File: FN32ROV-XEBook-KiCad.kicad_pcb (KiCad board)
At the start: 2 copper layers, 66 x 56 mm, 64 parts, among them J2 USB-C 16P, Q1 UMH3NTN, Q2 DMP2035U-7, Q3 DMG2302U, U1 ESP32-WROVER-IE-N16R8, U2 CP2102N-A02-GQFN24R, U3 74LS07DR, U4 74LS07DR, U5 XC6220B331MR

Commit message: Resize R13 to 2.7k for the LED boards green WiFi LED, document the LED board interface
The WiFi status LED moved to the new FN32ROV-XEBook-LED-KiCad daughter board and
changed color from white to green, which has a lower forward voltage (~2.2V vs
~2.9V). R13 needed to grow from 1k to 2.7k to keep the current in the same range
as the original design. Also documents the sibling LED board repo and the
per-channel resistor rationale in CLAUDE.md.

Co-Authored-By: Claude Sonnet 5 <noreply@anthropic.com>
Claude-Session: https://claude.ai/code/session_011E5FphyrLWBpYvbXpCPZfr
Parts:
- R13: value 1k -> 2.7k
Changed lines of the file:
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@@
 			)
 		)
-		(property "Value" "1k"
+		(property "Value" "2.7k"
 			(at 0 1.17 0)
 			(layer "F.Fab")
+			(hide yes)
 			(effects
 				(font
@@
 			(at 0 1.17 0)
 			(layer "F.Fab")
-			(effects
-				(font
+			(hide yes)
+			(effects
+				(font

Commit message: Replace D7/D8 diode part to fix SOD-323/SOD-123W package mismatch
PCBWay's assembly review caught that PMEG2010ER,115 (the part specified
for D7/D8) is only manufactured in SOD-123W, not the SOD-323 footprint
used on this board. Rather than swap the PCB footprint (which would
require re-routing around a nearby USB_D+ trace and re-exporting
gerbers), swapped the part instead: Nexperia PMEG2010BEA,115
(LCSC C455041) is a direct electrical equivalent (20V/1A Schottky, low
Vf) genuinely packaged in SOD-323, matching the existing footprint.
Board layout and gerbers are unaffected (value text lives on F.Fab).

Also includes the filled-in Customer Reply column for PCBWay's BOM
quote questions (this diode fix, three benign capacitor voltage-rating
upgrades, sourcing for J_SIO1, and flagging that their R13 quote used a
stale pre-2.7k BOM revision).

Co-Authored-By: Claude Sonnet 5 <noreply@anthropic.com>
Claude-Session: https://claude.ai/code/session_01GM9FQ1pLMMKCV3Qfiq1ore
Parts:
- D7, D8: value PMEG2010ER,115 -> PMEG2010BEA,115
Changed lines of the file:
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@@
 			(at 0 3.23 0)
 			(layer "F.Fab")
+			(hide yes)
 			(effects
 				(font
@@
 			)
 		)
-		(property "Value" "PMEG2010ER,115"
+		(property "Value" "PMEG2010BEA,115"
 			(at 0.1 1.9 90)
 			(layer "F.Fab")
@@
 			)
 		)
-		(property "Value" "PMEG2010ER,115"
+		(property "Value" "PMEG2010BEA,115"
 			(at 0.1 1.9 90)
 			(layer "F.Fab")

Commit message: Ground the copper pour, finish the plane, and archive the as-built 1.0 package
The single F.Cu/B.Cu zone was (net 0) -- a floating flood, not a ground plane.
Assign it to /GND and complete it:

- 65 stitching vias on a 3mm grid (GND vias 4 -> 177), placed by deflating the
  filled zone polygon 0.75mm per layer and intersecting F.Cu with B.Cu, so every
  candidate is inherently clearance-safe
- island_removal_mode -> Always, clearing 67 isolated_copper warnings
- min_resolved_spokes 2 -> 1; D4.2 and C4.1 set to solid zone connection

81 -> 8 DRC violations, 0 unconnected. Strictly additive: 64 footprint positions
byte-identical, tracks 894 -> 894, outline 66.050 x 56.050mm unchanged to 0.1um,
because the mounting brackets are already fabricated.

Fab/ restructured: the exact package sent to PCBWay is frozen under
as-built-1.0-PCBWay-T-1D22W845207A/ with the quote correspondence, and the new
Gerbers-FN32ROV-XEBook-1.1/ sits alongside it. 1.1 differs from 1.0 only in
F.Cu, B.Cu and the PTH drill (+65 hits); mask, paste, silkscreen and Edge.Cuts
are byte-identical, and BOM/CPL are copied verbatim.

PCBWay declined the mid-order swap on 2026-08-02 -- the boards were already in
manufacturing -- so 1.1 has never been fabricated and is future-order-only.
The ordered boards still work: verified 0 unconnected, 59 GND pads tied by 188
track/via segments. GND was fully routed in copper precisely because the pour
carried no net, so nothing depended on it.

Also adds the SIO/SD cable wiring PDFs under Docs/.

Co-Authored-By: Claude Opus 5 <noreply@anthropic.com>
Claude-Session: https://claude.ai/code/session_01VRTanwY2PaFNJQ1vUGmami
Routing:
- net /GND: vias 4 -> 69
- added copper zone on B.Cu, net /GND
- added copper zone on F.Cu, net /GND
- removed copper zone on B.Cu, net (none)
- removed copper zone on F.Cu, net (none)

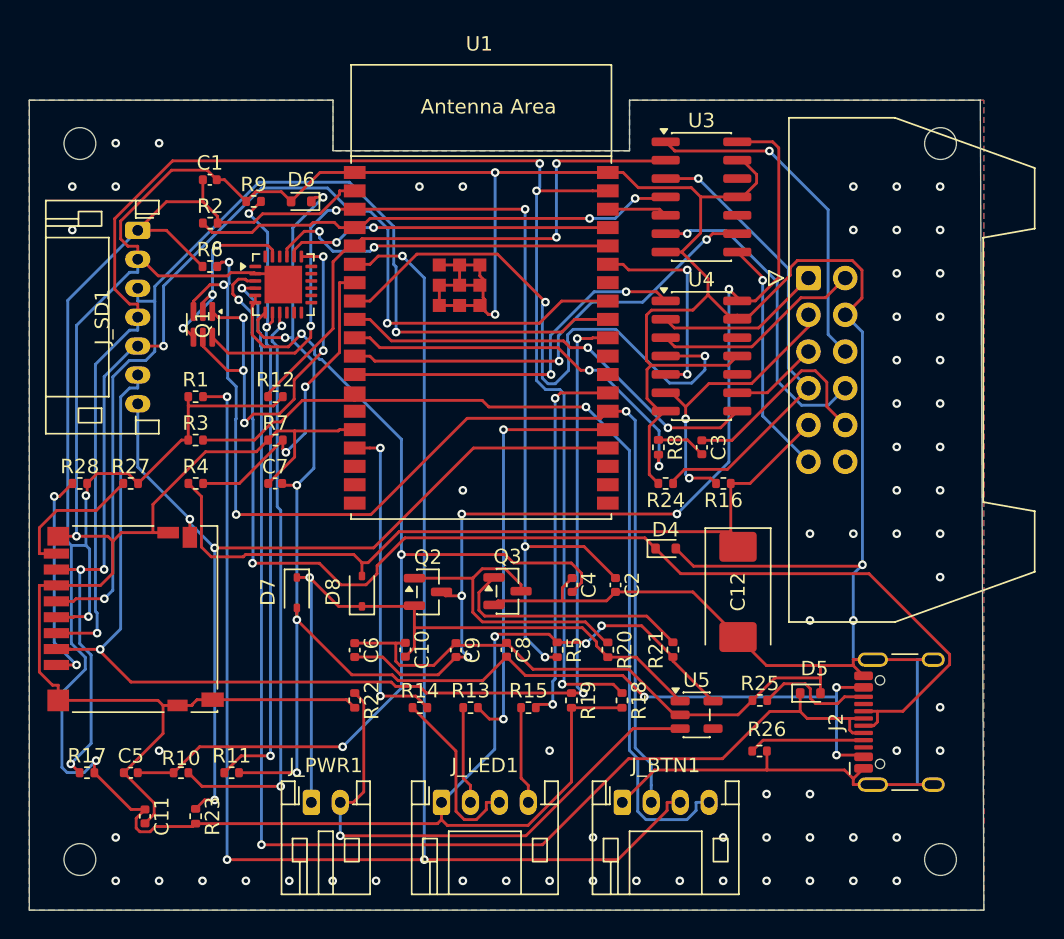
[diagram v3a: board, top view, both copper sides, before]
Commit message: Match LED brightness (R14 30k, R15 10K) and re-export fab for PCBWay
WiFi (R13 2.7k, green) was the channel the build is happy with; BT and SIO
read about twice as bright. Values come from a bench match on the LED board
at 3.33V with WiFi through its real 2.7k, not from calculation -- estimates
based on the 50%-dimming tape used as a stopgap landed near 2.4k and were
far off. The visual match was 9.2k on SIO; 10K was chosen deliberately as
slightly dimmer and already a basic part on this board.

  R13 WiFi green   2.7k  unchanged  C413089
  R14 BT   blue    1k -> 30k        C25776
  R15 SIO  orange  1.2k -> 10K      C25744

The 1.0 boards still carry 1k/1.2k and need hand-rework (0402s at y=67).

Fab re-export (Gerbers-FN32ROV-XEBook-1.1, never fabricated, so updated in
place): copper and drill came out identical to the 2026-08-01 export, which
also confirms the post-autoroute copper restore is exact. Only F.Silkscreen
changed, picking up the D4-D8 cathode bars and the corrected J_SIO1 vertical
header that were fixed in source after that export. Pick-and-place positions
and rotations are unchanged from what PCBWay assembled on 1.0.

Adds FN32ROV-XEBook-KiCad-BOM-PCBWay.xlsx/.csv as the file to send PCBWay:
same-part designators on one row (their explicit request), actual purchased
MPNs, the higher-voltage caps they substituted, J_SIO1 as BOOMELE 2.54-2*6P
(C9136), R13 on its own line. Verified against the schematic BOM and
pick-and-place: 60 placements, 28 lines. The plain BOM is now exported from
the schematic rather than hand-maintained.

Also folds in uncommitted work from earlier sessions: U1 -> ESP32-WROVER-E-
N16R8 (C529589) for the working PCB antenna, J_SIO1 -> Connector_IDC vertical
footprint, the unused Latch_Horizontal override's silk, removal of the two
superseded cable PDFs, and PCBWay's rev-1.0 question photos (D4/D5/D6 and
J_SIO1 orientation). .dsn is now gitignored as a regenerable export.

Co-Authored-By: Claude Opus 5 (1M context) <noreply@anthropi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
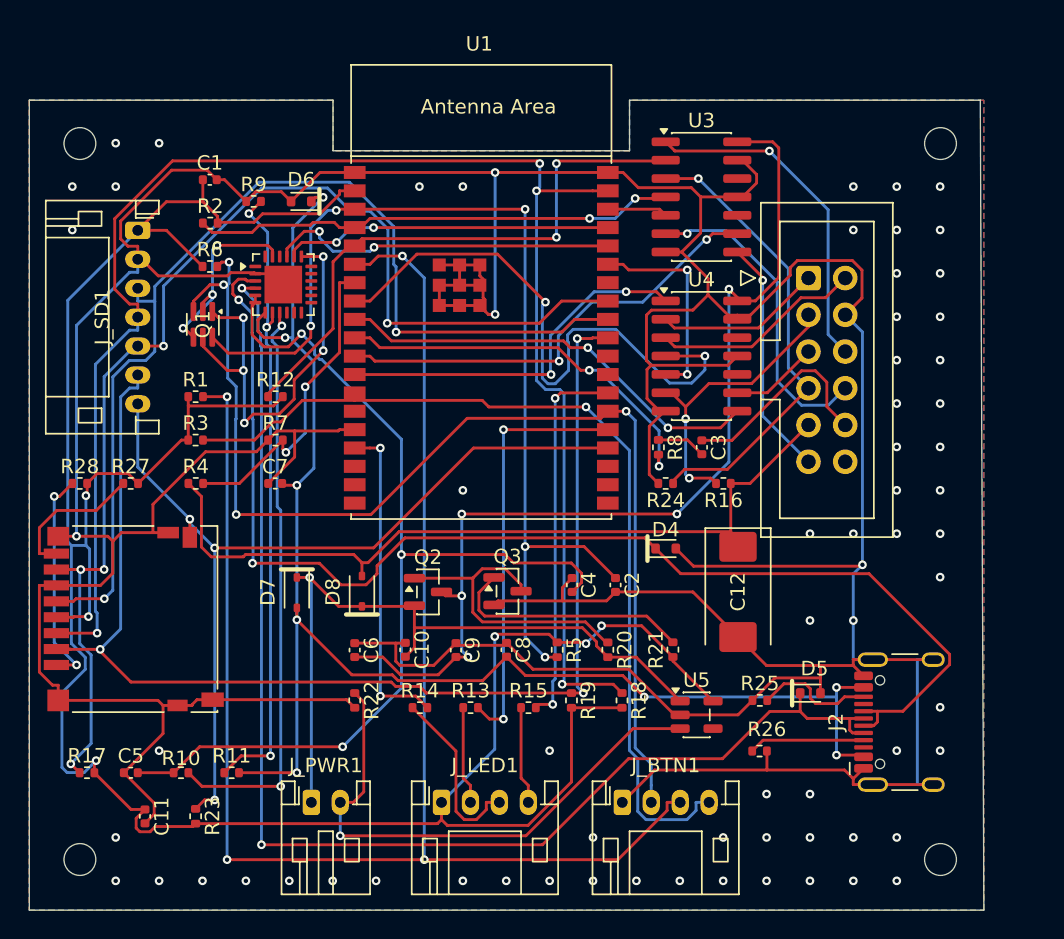
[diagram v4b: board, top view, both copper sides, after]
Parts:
- J_SIO1: footprint LocalOverrides:IDC-Header_2x06_P2.54mm_Latch_Horizontal -> Connector_IDC:IDC-Header_2x06_P2.54mm_Vertical
- R14: value 1k -> 30k
- R15: value 1.2k -> 10K
- U1: value ESP32-WROVER-IE-N16R8 -> ESP32-WROVER-E-N16R8
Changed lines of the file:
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@@
 		(attr smd)
 		(fp_line
-			(start -1.26 -0.6)
-			(end -1.26 0.6)
+			(start -1.26 -0.85)
+			(end -1.26 0.85)
 			(stroke
-				(width 0.12)
+				(width 0.3)
 				(type solid)
 			)
@@
 		)
 		(fp_line
-			(start -1.26 -0.6)
-			(end -1.26 0.6)
+			(start -1.26 -0.85)
+			(end -1.26 0.85)
 			(stroke
-				(width 0.12)
+				(width 0.3)
 				(type solid)
 			)
@@
 			)
 		)
-		(property "Value" "1.2k"
+		(property "Value" "10K"
 			(at 0 3.23 0)
 			(layer "F.Fab")
@@
 		(attr smd)
 		(fp_line
-			(start -1.61 -0.85)
-			(end 1.05 -0.85)
+			(start -1.61 -1.1)
+			(end -1.61 1.1)
 			(stroke
-				(width 0.12)
+				(width 0.3)
 				(type solid)
 			)
@@
 		(fp_line
 			(start -1.61 -0.85)
-			(end -1.61 0.85)
+			(end 1.05 -0.85)
 			(stroke
 				(width 0.12)
@@
 		(attr smd)
 		(fp_line
-			(start -1.26 -0.6)
-			(end -1.26 0.6)
+			(start -1.26 -0.85)
+			(end -1.26 0.85)
 			(stroke
-				(width 0.12)
+				(width 0.3)
 				(type solid)
 			)
@@
 		)
 	)
-	(footprint "LocalOverrides:IDC-Header_2x06_P2.54mm_Latch_Horizontal"
+	(footprint "Connector_IDC:IDC-Header_2x06_P2.54mm_Vertical"
 		(layer "F.Cu")
 		(at 72.8725 37.3)
@@
 		(attr through_hole)
 		(fp_line
-			(start -2.74 -0.5)
-			(end -2.74 0.5)
+			(start -4.68 -0.5)
+			(end -4.68 0.5)
 			(stroke
 				(width 0.12)
@@
 		)
 		(fp_line
-			(start -2.74 0.5)
-			(end -1.74 0)
+			(start -4.68 0.5)
+			(end -3.68 0)
 			(stroke
 				(width 0.12)
@@
 		)
 		(fp_line
-			(start -1.74 0)
-			(end -2.74 -0.5)
+			(start -3.68 0)
+			(end -4.68 -0.5)
 			(stroke
 				(width 0.12)
@@
 		)
 		(fp_line
-			(start -1.35 -11.08)
-			(end 5.98 -11.08)
+			(start -3.29 -5.21)
+			(end 5.83 -5.21)
 			(stroke
 				(width 0.12)
@@
 		)
 		(fp_line
-			(start -1.35 23.78)
-			(end -1.35 -11.08)
+			(start -3.29 4.3)
+			(end -1.98 4.3)
 			(stroke
 				(width 0.12)
@@
 		)
 		(fp_line
-			(start 5.98 -11.08)
-			(end 15.64 -7.61)
+			(start -3.29 17.91)
+			(end -3.29 -5.21)
 			(stroke
 				(width 0.12)
@@
 		)
 		(fp_line
-			(start 5.98 23.78)
-			(end -1.35 23.78)
+			(start -1.98 -3.91)
+			(end 4.52 -3.91)
 			(stroke
 				(width 0.12)
@@
 		)
 		(fp_line
-			(start 12.08 -2.79)
-			(end 12.08 15.49)
+			(start -1.98 4.3)
+			(end -1.98 -3.91)
 			(stroke
 				(width 0.12)
@@
 		)
 		(fp_line
-			(start 12.08 15.49)
-			(end 15.64 16.12)
+			(start -1.98 8.4)
+			(end -3.29 8.4)
 			(stroke
 				(width 0.12)
@@
 		)
 		(fp_line
-			(start 15.64 -7.61)
-			(end 15.64 -3.42)
+			(start -1.98 16.61)
+			(end -1.98 8.4)
 			(stroke
 				(width 0.12)
@@
 		)
 		(fp_line
-			(start 15.64 -3.42)
-			(end 12.08 -2.79)
+			(start 4.52 -3.91)
+			(end 4.52 16.61)
 			(stroke
 				(width 0.12)
@@
 		)
 		(fp_line
-			(start 15.64 16.12)
-			(end 15.64 20.31)
+			(start 4.52 16.61)
+			(end -1.98 16.61)
 			(stroke
 				(width 0.12)
@@
 		)
 		(fp_line
-			(start 15.64 20.31)
-			(end 5.98 23.78)
+			(start 5.83 -5.21)
+			(end 5.83 17.91)
+			(stroke
+				(width 0.12)
+				(type solid)
+			)
+			(layer "F.SilkS")
+		)
+		(fp_line
+			(start 5.83 17.91)
+			(end -3.29 17.91)
 			(stroke
 				(width 0.12)
@@
 		)
 		(fp_rect
-			(start -1.74 -11.47)
-			(end 16.03 24.17)
+			(start -3.68 -5.6)
+			(end 6.22 18.3)
 			(stroke
 				(width 0.05)
@@
 		)
 		(fp_line
-			(start -1.24 -10.97)
-			(end 5.87 -10.97)
+			(start -3.18 -4.1)
+			(end -2.18 -5.1)
 			(stroke
 				(width 0.1)
@@
 		)
 		(fp_line
-			(start -1.24 23.67)
-			(end -1.24 -10.97)
+			(start -3.18 4.3)
+			(end -1.98 4.3)
 			(stroke
 				(width 0.1)
@@
 		)
 		(fp_line
-			(start 5.87 -10.97)
-			(end 15.53 -7.5)
+			(start -3.18 17.8)
+			(end -3.18 -4.1)
 			(stroke
 				(width 0.1)
@@
 		)
 		(fp_line
-			(start 5.87 23.67)
-			(end -1.24 23.67)
+			(start -2.18 -5.1)
+			(end 5.72 -5.1)
 			(stroke
 				(width 0.1)
@@
 		)
 		(fp_line
-			(start 11.97 -2.9)
-			(end 11.97 15.6)
+			(start -1.98 -3.91)
+			(end 4.52 -3.91)
 			(stroke
 				(width 0.1)
@@
 		)
 		(fp_line
-			(start 11.97 15.6)
-			(end 15.53 16.23)
+			(start -1.98 4.3)
+			(end -1.98 -3.91)
 			(stroke
 				(width 0.1)
@@
 		)
 		(fp_line
-			(start 15.53 -7.5)
-			(end 15.53 -3.53)
+			(start -1.98 8.4)
+			(end -3.18 8.4)
 			(stroke
 				(width 0.1)
@@
 		)
 		(fp_line
-			(start 15.53 -3.53)
-			(end 11.97 -2.9)
+			(start -1.98 16.61)
+			(end -1.98 8.4)
 			(stroke
 				(width 0.1)
@@
 		)
 		(fp_line
-			(start 15.53 16.23)
-			(end 15.53 20.2)
+			(start 4.52 -3.91)
+			(end 4.52 16.61)
 			(stroke
 				(width 0.1)
@@
 		)
 		(fp_line
-			(start 15.53 20.2)
-			(end 5.87 23.67)
+			(start 4.52 16.61)
+			(end -1.98 16.61)
+			(stroke
+				(width 0.1)
+				(type solid)
+			)
+			(layer "F.Fab")
+		)
+		(fp_line
+			(start 5.72 -5.1)
+			(end 5.72 17.8)
+			(stroke
+				(width 0.1)
+				(type solid)
+			)
+			(layer "F.Fab")
+		)
+		(fp_line
+			(start 5.72 17.8)
+			(end -3.18 17.8)
 			(stroke
 				(width 0.1)
@@
 		)
 		(embedded_fonts no)
-		(model "${KICAD9_3DMODEL_DIR}/Connector_IDC.3dshapes/IDC-Header_2x06_P2.54mm_Horizontal.step"
+		(model "${KICAD9_3DMODEL_DIR}/Connector_IDC.3dshapes/IDC-Header_2x06_P2.54mm_Vertical.step"
 			(offset
 				(xyz 0 0 0)
@@
 			)
 		)
-		(property "Value" "1k"
+		(property "Value" "30k"
 			(at 0 1.17 0)
 			(layer "F.Fab")
@@
 		(fp_line
 			(start -1.61 -0.85)
-			(end -1.61 0.85)
+			(end 1.05 -0.85)
 			(stroke
 				(width 0.12)
@@
 		)
 		(fp_line
-			(start -1.61 -0.85)
-			(end 1.05 -0.85)
+			(start -1.61 -1.1)
+			(end -1.61 1.1)
 			(stroke
-				(width 0.12)
+				(width 0.3)
 				(type solid)
 			)
@@
 			)
 		)
-		(property "Value" "ESP32-WROVER-IE-N16R8"
+		(property "Value" "ESP32-WROVER-E-N16R8"
 			(at -0.095 17.78 0)
 			(layer "F.Fab")
